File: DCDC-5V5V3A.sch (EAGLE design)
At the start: 34 parts, among them U1 TPS63020DSJR

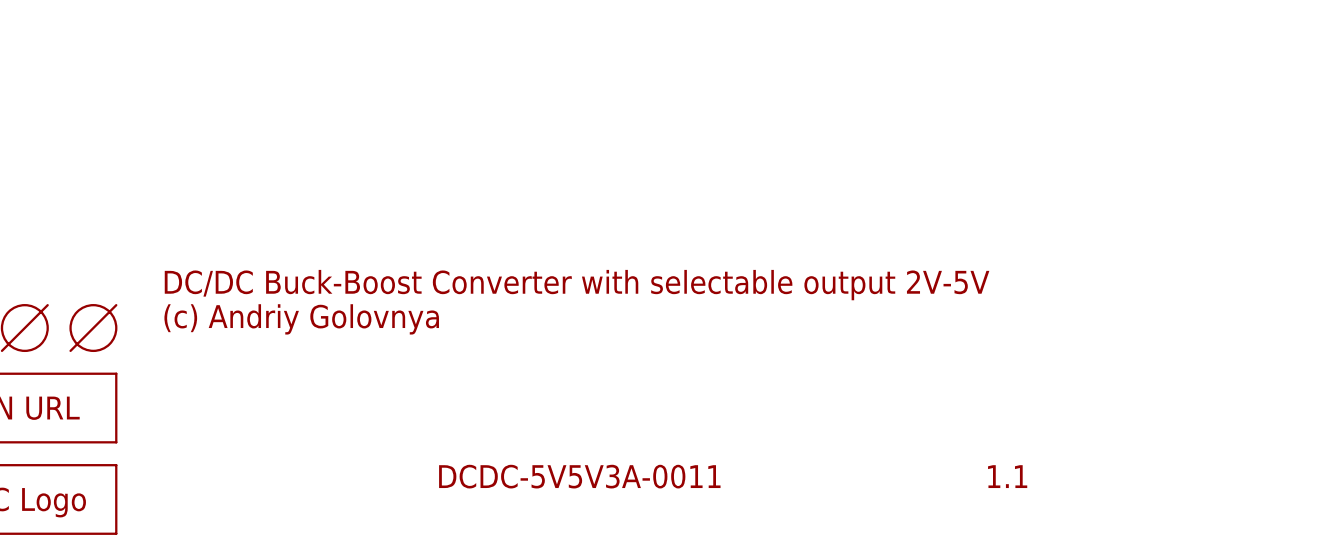
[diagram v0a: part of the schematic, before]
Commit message: fixed schematics description. Generated PDF schematics.
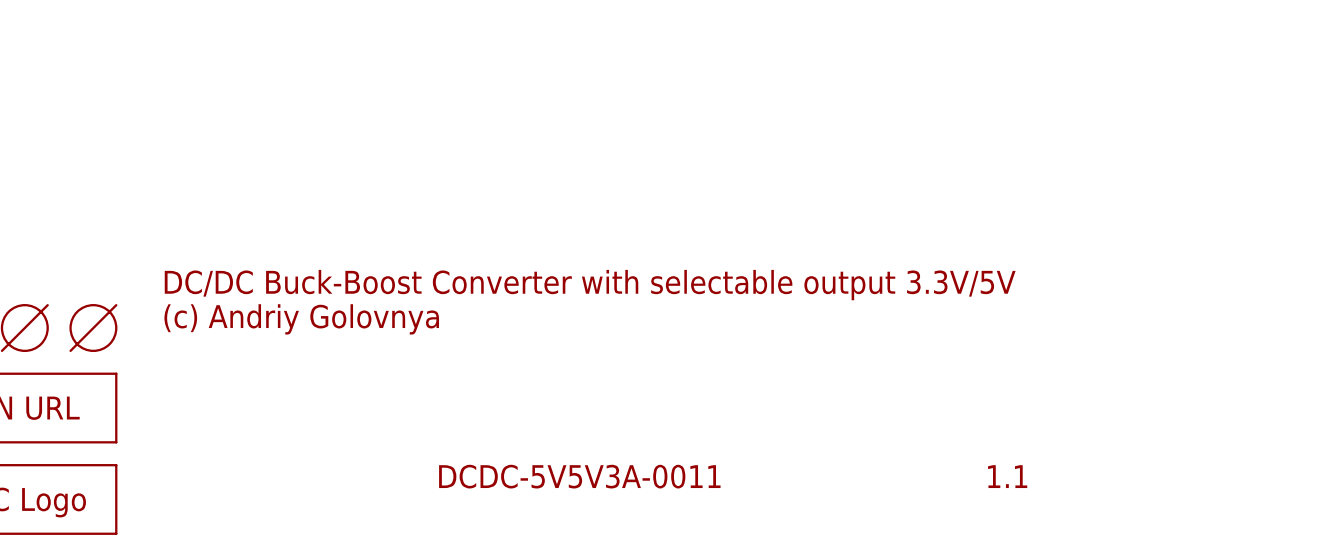
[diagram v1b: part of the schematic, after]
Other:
- note added: "DC/DC Buck-Boost Converter with selectable output 3.3V/5V (c) Andriy Golovnya"
- note removed: "DC/DC Buck-Boost Converter with selectable output 2V-5V (c) Andriy Golovnya"
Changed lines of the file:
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@@
 <text x="256.54" y="7.62" size="2.54" layer="94">1.1</text>
 <text x="195.58" y="7.62" size="2.54" layer="94">DCDC-5V5V3A-0011</text>
-<text x="165.1" y="25.4" size="2.54" layer="94">DC/DC Buck-Boost Converter with selectable output 2V-5V
+<text x="165.1" y="25.4" size="2.54" layer="94">DC/DC Buck-Boost Converter with selectable output 3.3V/5V
 (c) Andriy Golovnya</text>
 <text x="99.06" y="137.16" size="2.54" layer="94">Vin to Vout Conversion</text>
